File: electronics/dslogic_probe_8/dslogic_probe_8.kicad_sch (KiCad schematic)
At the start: 16 parts, among them J1 Conn_02x04_Odd_Even, J2 Conn_02x04_Odd_Even

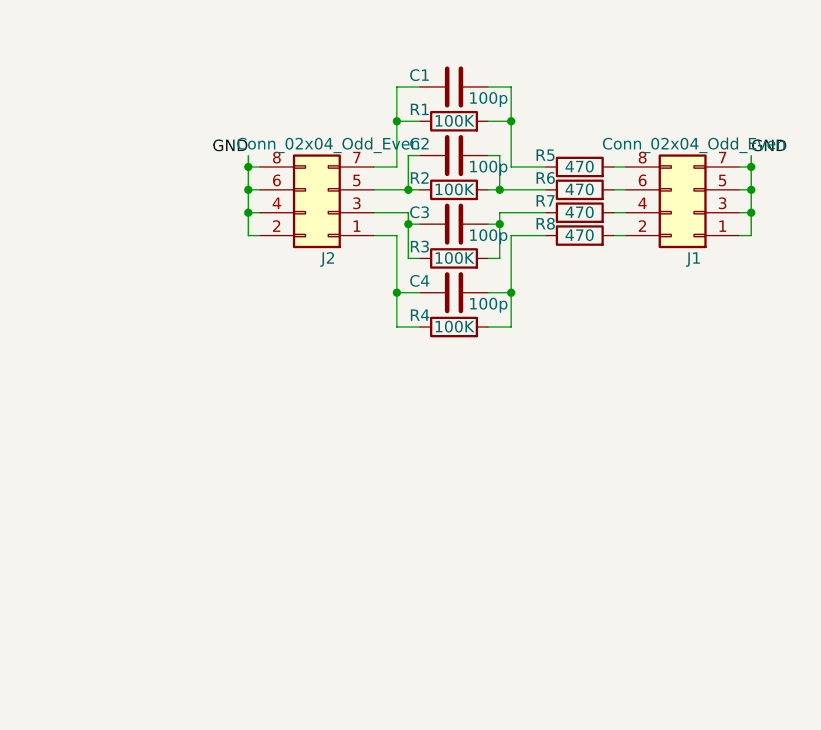
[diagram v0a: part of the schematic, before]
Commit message: updated to 8 channels
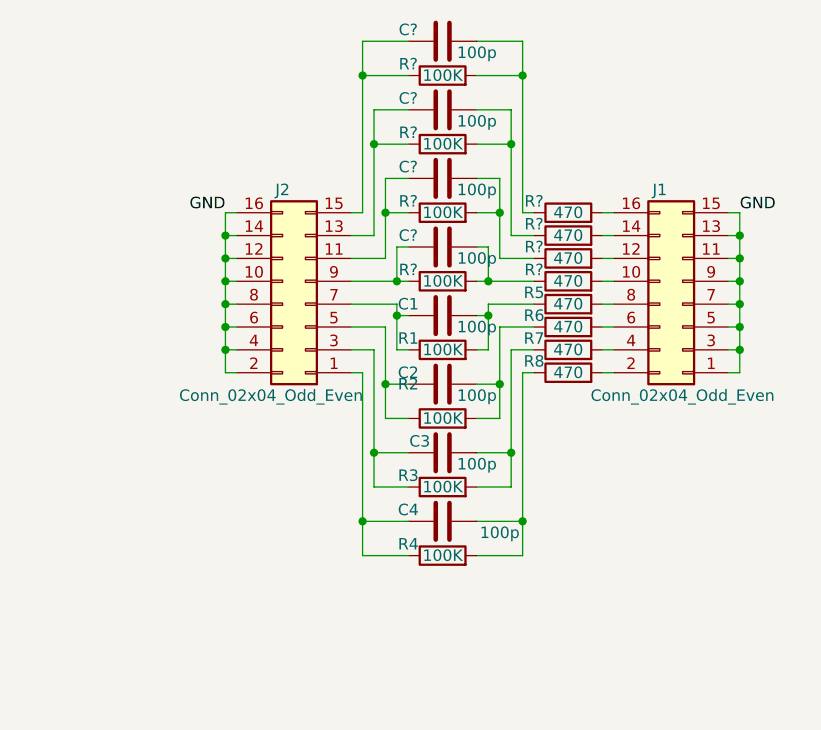
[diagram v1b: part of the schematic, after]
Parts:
- added C? (x4): 100p, SquantorRcl:C_0402, symbol Device:C
- added R? (x4): 470, SquantorRcl:R_0402_hand, symbol Device:R
- added R? (x4): 100K, SquantorRcl:R_0402_hand, symbol Device:R
- J1, J2: symbol Connector_Generic:Conn_02x04_Odd_Even -> Connector_Generic:Conn_02x08_Odd_Even
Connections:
- net GND: now also J1.11 (Pin_11), J1.13 (Pin_13), J1.15 (Pin_15), J1.9 (Pin_9), J2.10 (Pin_10), J2.12 (Pin_12), J2.14 (Pin_14), J2.16 (Pin_16)
- new net: C?.2, R?.1, R?.2 (x4)
- new net: J1.16 (Pin_16), R?.2
- new net: C?.1, J2.9 (Pin_9), R?.1
- new net: C?.1, J2.11 (Pin_11), R?.1
- new net: C?.1, J2.13 (Pin_13), R?.1
- new net: C?.1, J2.15 (Pin_15), R?.1
- new net: J1.10 (Pin_10), R?.2
- new net: J1.12 (Pin_12), R?.2
- new net: J1.14 (Pin_14), R?.2
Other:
- moved on the sheet: C1, C2, C3, C4, R1, R2, R3, R4, R5, R6, R7, R8

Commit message: WIP routing and placing
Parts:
- gave numbers to parts that had none: 12
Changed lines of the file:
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@@
   (symbol (lib_id "Device:R") (at 100.33 40.64 90) (unit 1)
     (in_bom yes) (on_board yes)
-    (property "Reference" "R?" (id 0) (at 96.52 39.37 90))
+    (property "Reference" "R13" (id 0) (at 96.52 39.37 90))
     (property "Value" "470" (id 1) (at 100.33 40.64 90))
     (property "Footprint" "SquantorRcl:R_0402_hand" (id 2) (at 100.33 42.418 90)
@@
   (symbol (lib_id "Device:C") (at 86.36 44.45 90) (unit 1)
     (in_bom yes) (on_board yes)
-    (property "Reference" "C?" (id 0) (at 82.55 43.18 90))
+    (property "Reference" "C8" (id 0) (at 82.55 43.18 90))
     (property "Value" "100p" (id 1) (at 90.17 45.72 90))
     (property "Footprint" "SquantorRcl:C_0402" (id 2) (at 90.17 43.4848 0)
@@
   (symbol (lib_id "Device:R") (at 86.36 40.64 90) (unit 1)
     (in_bom yes) (on_board yes)
-    (property "Reference" "R?" (id 0) (at 82.55 39.37 90))
+    (property "Reference" "R11" (id 0) (at 82.55 39.37 90))
     (property "Value" "100K" (id 1) (at 86.36 40.64 90))
     (property "Footprint" "SquantorRcl:R_0402_hand" (id 2) (at 86.36 42.418 90)
@@
   (symbol (lib_id "Device:C") (at 86.36 21.59 90) (unit 1)
     (in_bom yes) (on_board yes)
-    (property "Reference" "C?" (id 0) (at 82.55 20.32 90))
+    (property "Reference" "C5" (id 0) (at 82.55 20.32 90))
     (property "Value" "100p" (id 1) (at 90.17 22.86 90))
     (property "Footprint" "SquantorRcl:C_0402" (id 2) (at 90.17 20.6248 0)
@@
   (symbol (lib_id "Device:R") (at 100.33 48.26 90) (unit 1)
     (in_bom yes) (on_board yes)
-    (property "Reference" "R?" (id 0) (at 96.52 46.99 90))
+    (property "Reference" "R16" (id 0) (at 96.52 46.99 90))
     (property "Value" "470" (id 1) (at 100.33 48.26 90))
     (property "Footprint" "SquantorRcl:R_0402_hand" (id 2) (at 100.33 50.038 90)
@@
   (symbol (lib_id "Device:R") (at 86.36 33.02 90) (unit 1)
     (in_bom yes) (on_board yes)
-    (property "Reference" "R?" (id 0) (at 82.55 31.75 90))
+    (property "Reference" "R10" (id 0) (at 82.55 31.75 90))
     (property "Value" "100K" (id 1) (at 86.36 33.02 90))
     (property "Footprint" "SquantorRcl:R_0402_hand" (id 2) (at 86.36 34.798 90)
@@
   (symbol (lib_id "Device:R") (at 100.33 45.72 90) (unit 1)
     (in_bom yes) (on_board yes)
-    (property "Reference" "R?" (id 0) (at 96.52 44.45 90))
+    (property "Reference" "R15" (id 0) (at 96.52 44.45 90))
     (property "Value" "470" (id 1) (at 100.33 45.72 90))
     (property "Footprint" "SquantorRcl:R_0402_hand" (id 2) (at 100.33 47.498 90)
@@
   (symbol (lib_id "Device:R") (at 86.36 25.4 90) (unit 1)
     (in_bom yes) (on_board yes)
-    (property "Reference" "R?" (id 0) (at 82.55 24.13 90))
+    (property "Reference" "R9" (id 0) (at 82.55 24.13 90))
     (property "Value" "100K" (id 1) (at 86.36 25.4 90))
     (property "Footprint" "SquantorRcl:R_0402_hand" (id 2) (at 86.36 27.178 90)
@@
   (symbol (lib_id "Device:R") (at 86.36 48.26 90) (unit 1)
     (in_bom yes) (on_board yes)
-    (property "Reference" "R?" (id 0) (at 82.55 46.99 90))
+    (property "Reference" "R12" (id 0) (at 82.55 46.99 90))
     (property "Value" "100K" (id 1) (at 86.36 48.26 90))
     (property "Footprint" "SquantorRcl:R_0402_hand" (id 2) (at 86.36 50.038 90)
@@
   (symbol (lib_id "Device:C") (at 86.36 29.21 90) (unit 1)
     (in_bom yes) (on_board yes)
-    (property "Reference" "C?" (id 0) (at 82.55 27.94 90))
+    (property "Reference" "C6" (id 0) (at 82.55 27.94 90))
     (property "Value" "100p" (id 1) (at 90.17 30.48 90))
     (property "Footprint" "SquantorRcl:C_0402" (id 2) (at 90.17 28.2448 0)
@@
   (symbol (lib_id "Device:R") (at 100.33 43.18 90) (unit 1)
     (in_bom yes) (on_board yes)
-    (property "Reference" "R?" (id 0) (at 96.52 41.91 90))
+    (property "Reference" "R14" (id 0) (at 96.52 41.91 90))
     (property "Value" "470" (id 1) (at 100.33 43.18 90))
     (property "Footprint" "SquantorRcl:R_0402_hand" (id 2) (at 100.33 44.958 90)
@@
   (symbol (lib_id "Device:C") (at 86.36 36.83 90) (unit 1)
     (in_bom yes) (on_board yes)
-    (property "Reference" "C?" (id 0) (at 82.55 35.56 90))
+    (property "Reference" "C7" (id 0) (at 82.55 35.56 90))
     (property "Value" "100p" (id 1) (at 90.17 38.1 90))
     (property "Footprint" "SquantorRcl:C_0402" (id 2) (at 90.17 35.8648 0)
@@
       (reference "C4") (unit 1) (value "100p") (footprint "SquantorRcl:C_0402")
     )
+    (path "/43b63f12-df85-4904-ac0b-761cb727a61e"
+      (reference "C5") (unit 1) (value "100p") (footprint "SquantorRcl:C_0402")
+    )
+    (path "/d8aeafd6-9aba-422c-920b-382f50343b7a"
+      (reference "C6") (unit 1) (value "100p") (footprint "SquantorRcl:C_0402")
+    )
+    (path "/f3391d26-9eaf-4d42-9e4e-b62c9056974d"
+      (reference "C7") (unit 1) (value "100p") (footprint "SquantorRcl:C_0402")
+    )
     (path "/20d90278-b27a-4766-a343-358d2c295604"
-      (reference "C?") (unit 1) (value "100p") (footprint "SquantorRcl:C_0402")
-    )
-    (path "/43b63f12-df85-4904-ac0b-761cb727a61e"
-      (reference "C?") (unit 1) (value "100p") (footprint "SquantorRcl:C_0402")
-    )
-    (path "/d8aeafd6-9aba-422c-920b-382f50343b7a"
-      (reference "C?") (unit 1) (value "100p") (footprint "SquantorRcl:C_0402")
-    )
-    (path "/f3391d26-9eaf-4d42-9e4e-b62c9056974d"
-      (reference "C?") (unit 1) (value "100p") (footprint "SquantorRcl:C_0402")
+      (reference "C8") (unit 1) (value "100p") (footprint "SquantorRcl:C_0402")
     )
     (path "/a72f7593-045b-4cee-9761-530bd4867197"
@@
       (reference "R8") (unit 1) (value "470") (footprint "SquantorRcl:R_0402_hand")
     )
+    (path "/ca7784ba-8cef-4e2a-9bd9-54d2ffce8772"
+      (reference "R9") (unit 1) (value "100K") (footprint "SquantorRcl:R_0402_hand")
+    )
+    (path "/94b8f17d-d350-422b-8463-568f89eb38d7"
+      (reference "R10") (unit 1) (value "100K") (footprint "SquantorRcl:R_0402_hand")
+    )
+    (path "/4161a3e3-29b1-452d-8675-a3460b8a5333"
+      (reference "R11") (unit 1) (value "100K") (footprint "SquantorRcl:R_0402_hand")
+    )
+    (path "/caf46713-94e6-44a5-a6e5-3ba829681797"
+      (reference "R12") (unit 1) (value "100K") (footprint "SquantorRcl:R_0402_hand")
+    )
     (path "/00928b25-6551-485c-8b2e-6a49ee515df9"
-      (reference "R?") (unit 1) (value "470") (footprint "SquantorRcl:R_0402_hand")
-    )
-    (path "/4161a3e3-29b1-452d-8675-a3460b8a5333"
-      (reference "R?") (unit 1) (value "100K") (footprint "SquantorRcl:R_0402_hand")
+      (reference "R13") (unit 1) (value "470") (footprint "SquantorRcl:R_0402_hand")
+    )
+    (path "/dbca477c-2c13-4d3e-a252-3beb034e395d"
+      (reference "R14") (unit 1) (value "470") (footprint "SquantorRcl:R_0402_hand")
+    )
+    (path "/9ee8eba8-0b77-4052-bdd7-799aa67085f4"
+      (reference "R15") (unit 1) (value "470") (footprint "SquantorRcl:R_0402_hand")
     )
     (path "/8ea2c05f-bc1d-43f9-ac98-3b140100ec39"
-      (reference "R?") (unit 1) (value "470") (footprint "SquantorRcl:R_0402_hand")
-    )
-    (path "/94b8f17d-d350-422b-8463-568f89eb38d7"
-      (reference "R?") (unit 1) (value "100K") (footprint "SquantorRcl:R_0402_hand")
-    )
-    (path "/9ee8eba8-0b77-4052-bdd7-799aa67085f4"
-      (reference "R?") (unit 1) (value "470") (footprint "SquantorRcl:R_0402_hand")
-    )
-    (path "/ca7784ba-8cef-4e2a-9bd9-54d2ffce8772"
-      (reference "R?") (unit 1) (value "100K") (footprint "SquantorRcl:R_0402_hand")
-    )
-    (path "/caf46713-94e6-44a5-a6e5-3ba829681797"
-      (reference "R?") (unit 1) (value "100K") (footprint "SquantorRcl:R_0402_hand")
-    )
-    (path "/dbca477c-2c13-4d3e-a252-3beb034e395d"
-      (reference "R?") (unit 1) (value "470") (footprint "SquantorRcl:R_0402_hand")
-    )
-  )
+      (reference "R16") (unit 1) (value "470") (footprint "SquantorRcl:R_0402_hand")
+    )
+  )

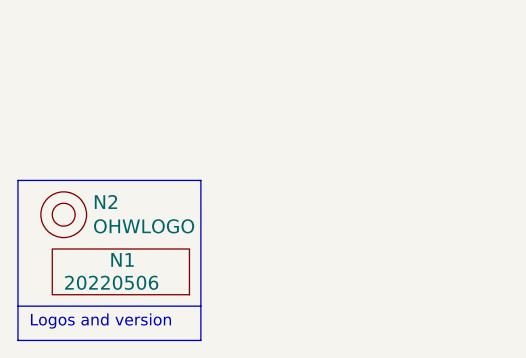
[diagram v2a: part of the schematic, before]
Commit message: WIP 8 channel dslogic probe
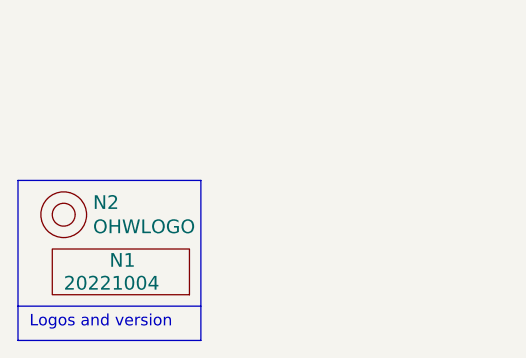
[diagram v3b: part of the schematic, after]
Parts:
- J1, J2: footprint SquantorConnectors:Header-0127-2X04-EDGE -> SquantorConnectors:Header-0127-2X08-EDGE
- N1: value 20220506 -> 20221004
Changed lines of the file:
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@@
       (effects (font (size 1.524 1.524)) (justify left))
     )
-    (property "Value" "20220506" (id 1) (at 20.32 189.23 0)
+    (property "Value" "20221004" (id 1) (at 20.32 189.23 0)
       (effects (font (size 1.524 1.524)) (justify left))
     )
@@
     (property "Reference" "J2" (id 0) (at 68.58 38.1 0))
     (property "Value" "Conn_02x04_Odd_Even" (id 1) (at 67.31 60.96 0))
-    (property "Footprint" "SquantorConnectors:Header-0127-2X04-EDGE" (id 2) (at 71.12 50.8 0)
+    (property "Footprint" "SquantorConnectors:Header-0127-2X08-EDGE" (id 2) (at 71.12 50.8 0)
       (effects (font (size 1.27 1.27)) hide)
     )
@@
     (property "Reference" "J1" (id 0) (at 110.49 38.1 0))
     (property "Value" "Conn_02x04_Odd_Even" (id 1) (at 113.03 60.96 0))
-    (property "Footprint" "SquantorConnectors:Header-0127-2X04-EDGE" (id 2) (at 113.03 50.8 0)
+    (property "Footprint" "SquantorConnectors:Header-0127-2X08-EDGE" (id 2) (at 113.03 50.8 0)
       (effects (font (size 1.27 1.27)) hide)
     )
@@
     )
     (path "/a72f7593-045b-4cee-9761-530bd4867197"
-      (reference "J1") (unit 1) (value "Conn_02x04_Odd_Even") (footprint "SquantorConnectors:Header-0127-2X04-EDGE")
+      (reference "J1") (unit 1) (value "Conn_02x04_Odd_Even") (footprint "SquantorConnectors:Header-0127-2X08-EDGE")
     )
     (path "/247d18a8-48ce-4e7f-9759-0eea4ad80e9a"
-      (reference "J2") (unit 1) (value "Conn_02x04_Odd_Even") (footprint "SquantorConnectors:Header-0127-2X04-EDGE")
+      (reference "J2") (unit 1) (value "Conn_02x04_Odd_Even") (footprint "SquantorConnectors:Header-0127-2X08-EDGE")
     )
     (path "/00000000-0000-0000-0000-00005ee12bf3"
-      (reference "N1") (unit 1) (value "20220506") (footprint "SquantorLabels:Label_Generic")
+      (reference "N1") (unit 1) (value "20221004") (footprint "SquantorLabels:Label_Generic")
     )
     (path "/00000000-0000-0000-0000-00005ee13678"

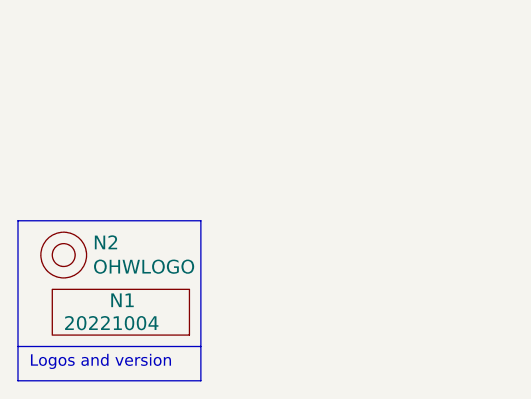
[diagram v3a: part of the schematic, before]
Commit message: fixed DRC issues with connectors
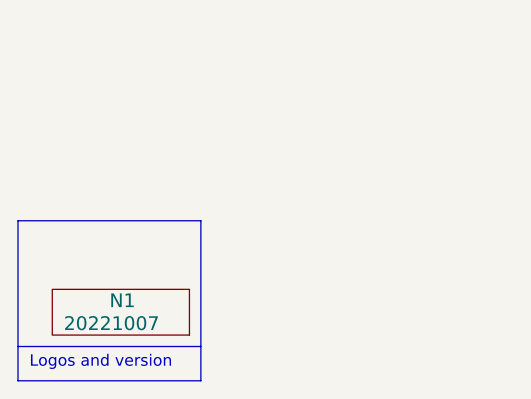
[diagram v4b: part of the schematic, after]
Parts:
- removed N2: OHWLOGO, Symbol:OSHW-Symbol_6.7x6mm_SilkScreen, symbol SquantorLabels:OHWLOGO
- N1: value 20221004 -> 20221007
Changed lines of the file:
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@@
       (effects (font (size 1.524 1.524)) (justify left))
     )
-    (property "Value" "20221004" (id 1) (at 20.32 189.23 0)
+    (property "Value" "20221007" (id 1) (at 20.32 189.23 0)
       (effects (font (size 1.524 1.524)) (justify left))
     )
@@
     )
     (property "Datasheet" "" (id 3) (at 26.67 189.23 0)
-      (effects (font (size 1.524 1.524)) hide)
-    )
-  )
-  (symbol (lib_id "SquantorLabels:OHWLOGO") (at 20.32 181.61 0) (unit 1)
-    (in_bom yes) (on_board yes)
-    (property "Reference" "N2" (id 0) (at 23.5712 180.2638 0)
-      (effects (font (size 1.524 1.524)) (justify left))
-    )
-    (property "Value" "OHWLOGO" (id 1) (at 23.5712 182.9562 0)
-      (effects (font (size 1.524 1.524)) (justify left))
-    )
-    (property "Footprint" "Symbol:OSHW-Symbol_6.7x6mm_SilkScreen" (id 2) (at 20.32 181.61 0)
-      (effects (font (size 1.524 1.524)) hide)
-    )
-    (property "Datasheet" "" (id 3) (at 20.32 181.61 0)
       (effects (font (size 1.524 1.524)) hide)
     )
@@
     )
     (path "/00000000-0000-0000-0000-00005ee12bf3"
-      (reference "N1") (unit 1) (value "20221004") (footprint "SquantorLabels:Label_Generic")
-    )
-    (path "/00000000-0000-0000-0000-00005ee13678"
-      (reference "N2") (unit 1) (value "OHWLOGO") (footprint "Symbol:OSHW-Symbol_6.7x6mm_SilkScreen")
+      (reference "N1") (unit 1) (value "20221007") (footprint "SquantorLabels:Label_Generic")
     )
     (path "/353cd110-9f23-4a67-ab3c-8758aad1b0ec"

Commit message: reviewed PCB and updated versionnumber
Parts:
- N1: value 20221007 -> 20221009
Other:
- note added: "Filtering circuit"
- moved on the sheet: C1, C2, C3, C4, C5, C6, C7, C8, J1, J2, R1, R10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
